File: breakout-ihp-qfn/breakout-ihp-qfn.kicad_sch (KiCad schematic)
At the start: 43 parts, among them J1 Conn_01x12, J2 DF12NB-60DS-0.5V_51, J3 DF12NB-50DS-0.5V_51, U1 AP2112K-1.2, U2 AP2112K-1.8, U3 TT_IHP_ASIC, U4 24LC02

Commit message: IHP schem title tweak
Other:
- note added: "QFN and Analog Breakout For TinyTapeout IHP ASICs"
- note removed: "QFN and Analog Breakout For TinyTapeout Skywater ASICs"
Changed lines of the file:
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@@
 		)
 	)
-	(text "QFN and Analog Breakout For TinyTapeout Skywater ASICs"
+	(text "QFN and Analog Breakout For TinyTapeout IHP ASICs"
 		(exclude_from_sim no)
 		(at 231.14 23.495 0)

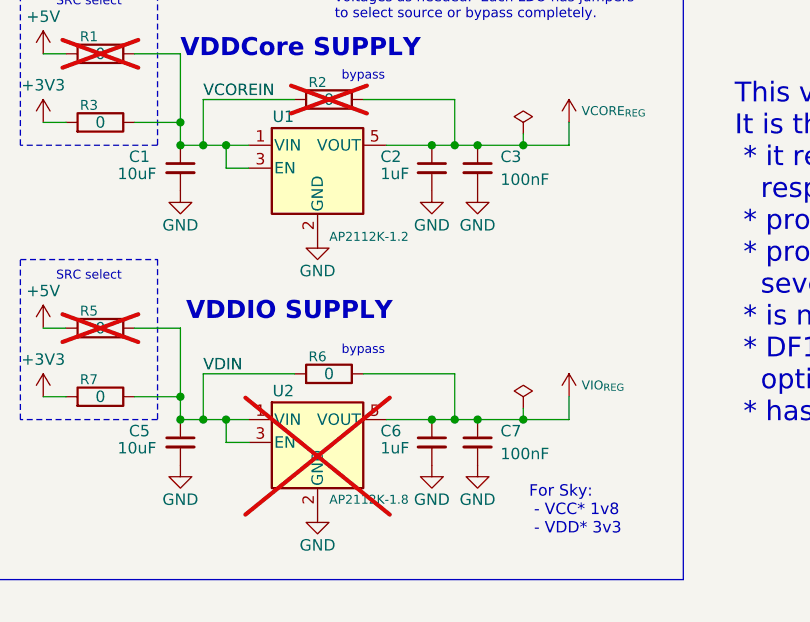
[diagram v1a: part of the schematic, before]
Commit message: IHP breakout rework from feedback
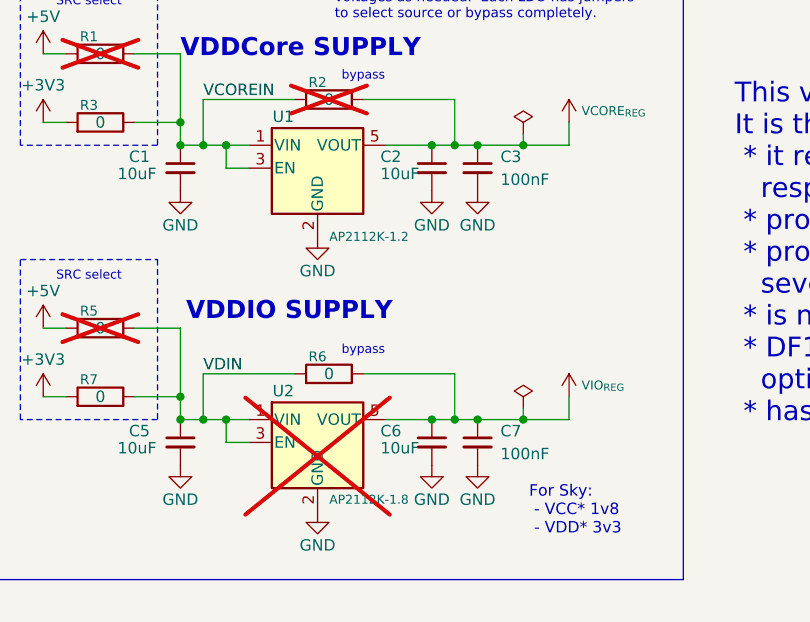
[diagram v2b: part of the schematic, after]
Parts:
- C1, C5: footprint Capacitor_SMD:C_0805_2012Metric -> Capacitor_SMD:C_0603_1608Metric; Characteristics 10u 10V XR 0805 -> 1u 10V XR 0603; LCSC C408142 -> (none); MPN GRM21BR71C106KE51L -> (none)
- C2, C6: value 1uF -> 10uF; LCSC C5673 -> (none); MPN GRT188R61H105KE13D -> (none)
- C4, C8, C9: value 1uF -> 10uF

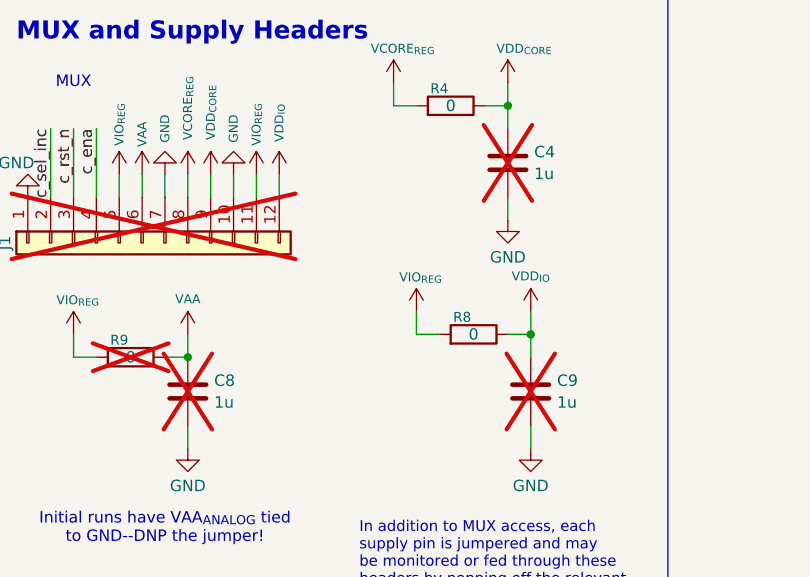
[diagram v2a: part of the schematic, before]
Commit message: 10u DNPs for IHP breakout
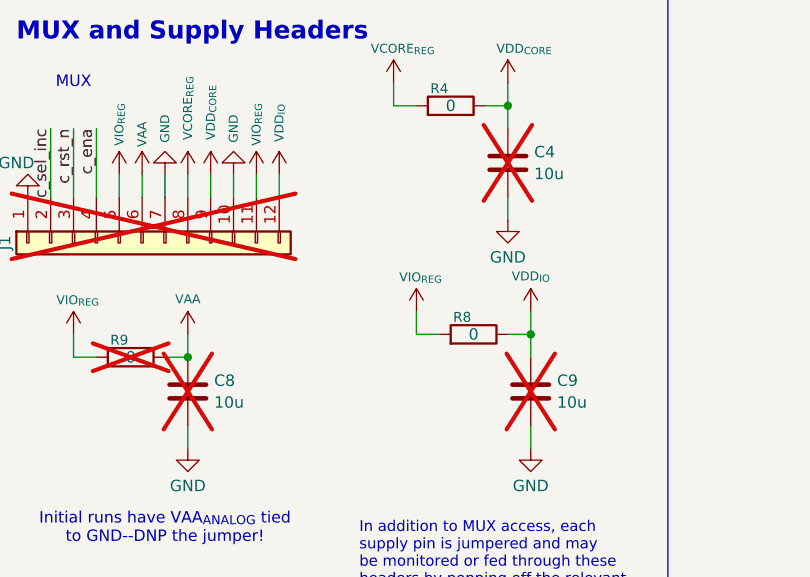
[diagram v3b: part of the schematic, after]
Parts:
- C4, C8, C9: Display Value 1u -> 10u
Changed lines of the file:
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@@
 			)
 		)
-		(property "Display Value" "1u"
+		(property "Display Value" "10u"
 			(at 320.421 88.8421 0)
 			(effects
@@
 			)
 		)
-		(property "Display Value" "1u"
+		(property "Display Value" "10u"
 			(at 317.881 63.4421 0)
 			(effects
@@
 			)
 		)
-		(property "Display Value" "1u"
+		(property "Display Value" "10u"
 			(at 282.321 88.8421 0)
 			(effects

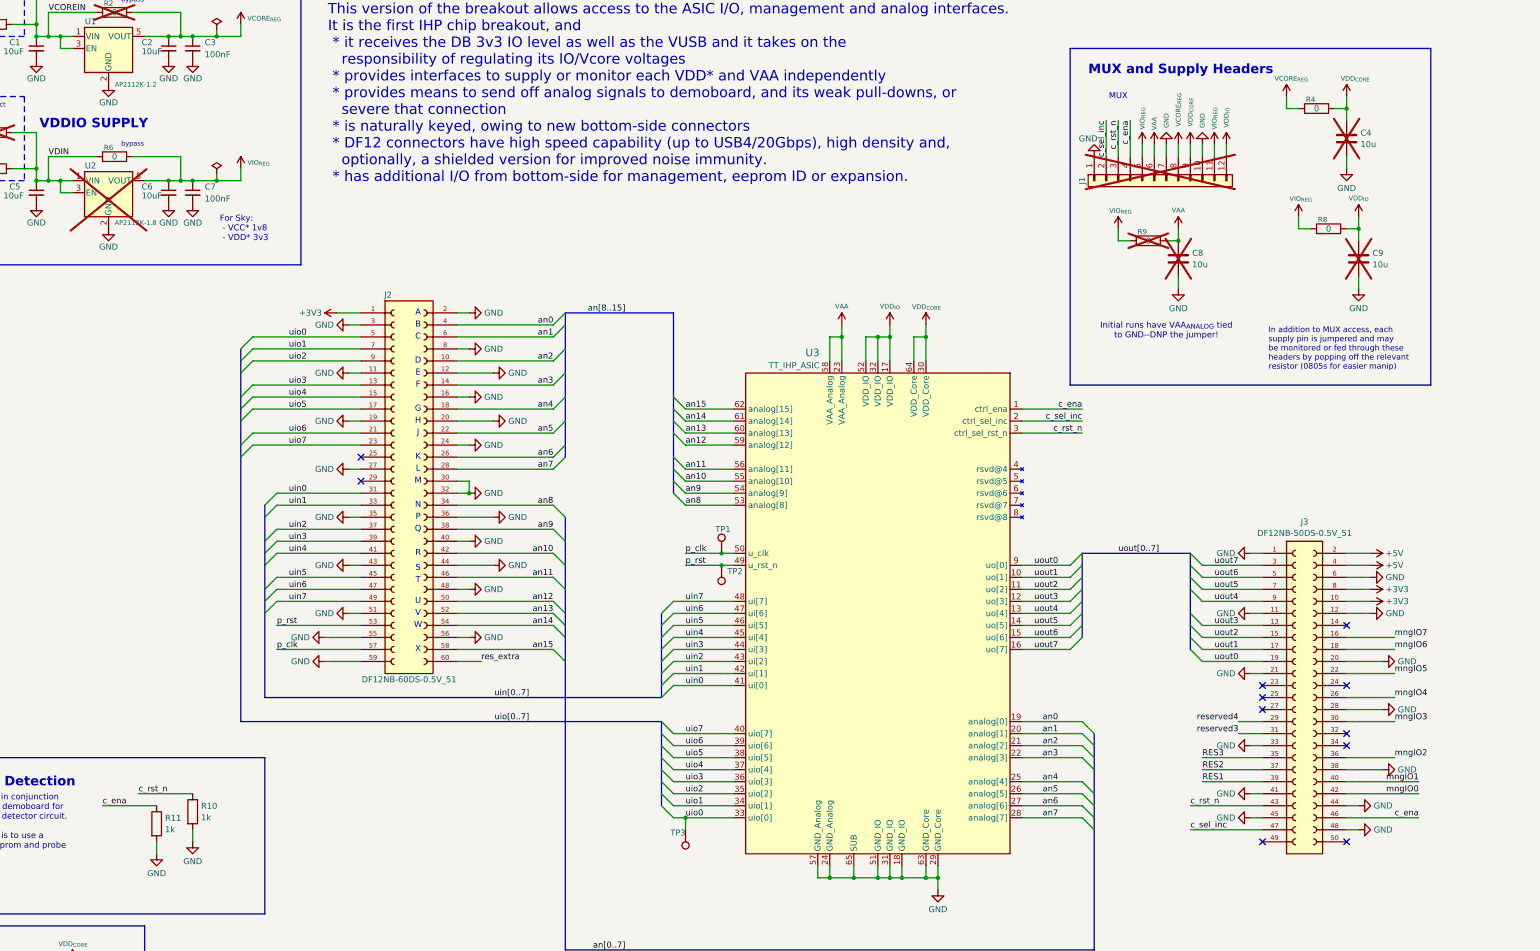
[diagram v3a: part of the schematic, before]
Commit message: schem cleanup/project mux bus renames
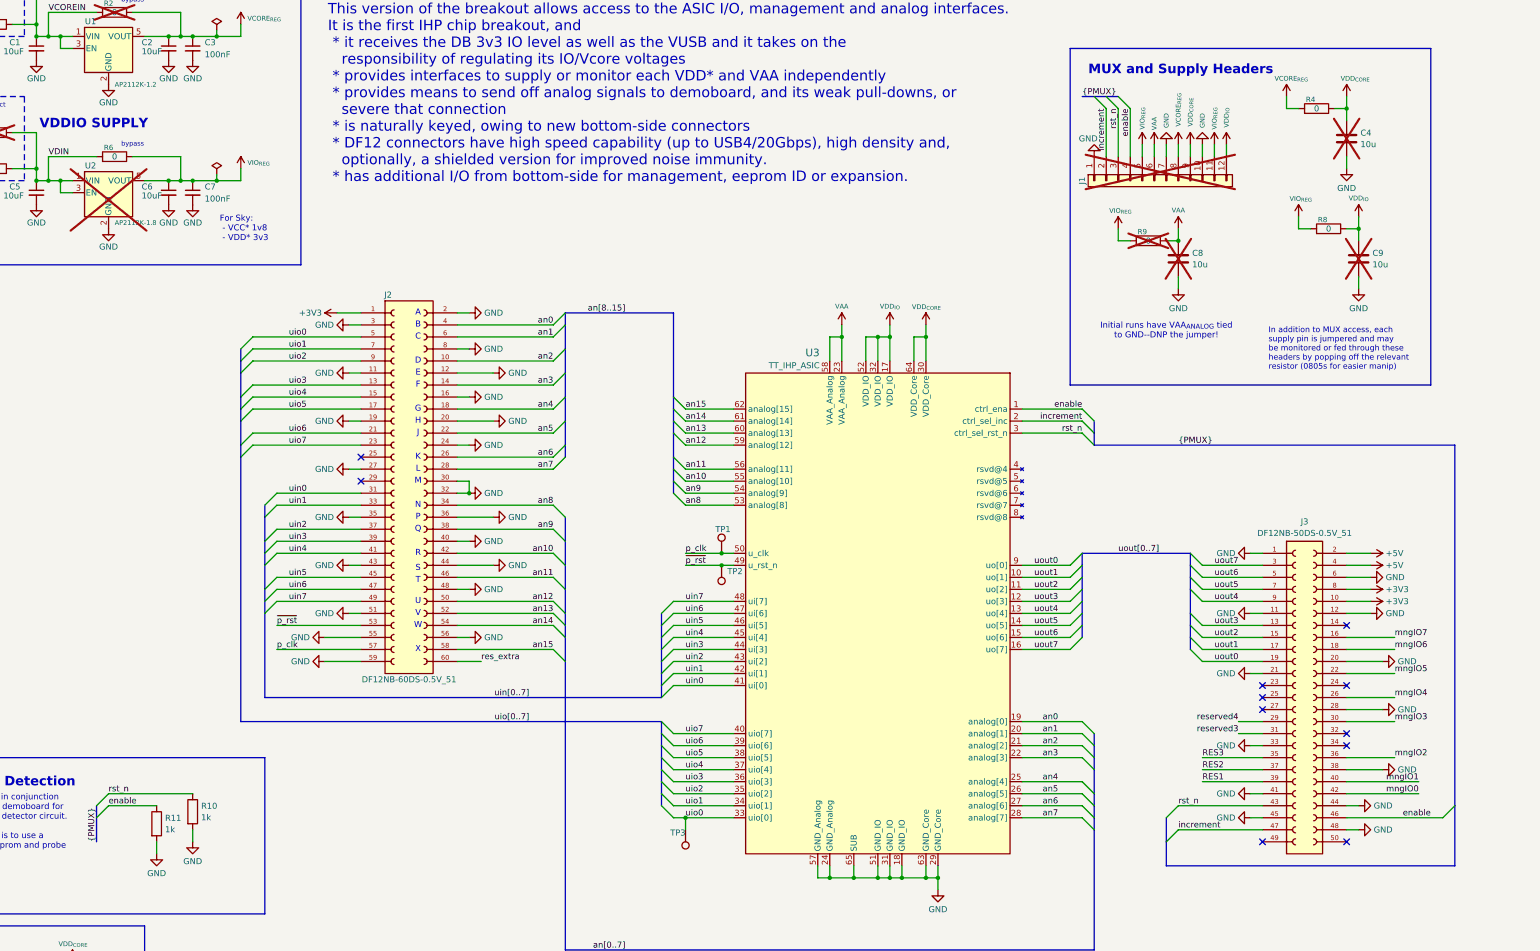
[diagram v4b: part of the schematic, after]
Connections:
- net c_ena renamed enable
- net c_rst_n renamed rst_n
- net c_sel_inc renamed increment
- net p_rst renamed ~{p_rst}
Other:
- note removed: "MUX"
